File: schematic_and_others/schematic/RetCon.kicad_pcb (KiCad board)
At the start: 2 copper layers, 139.5 x 70.4 mm, 36 parts, among them J1 Hole1, J2 Hole2, J3 Hole3, J4 Hole4, J5 programming port, J6 USB_B_Micro, SW1 SW_SPDT, SW2 Home, SW3 BumperR, SW4 Select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

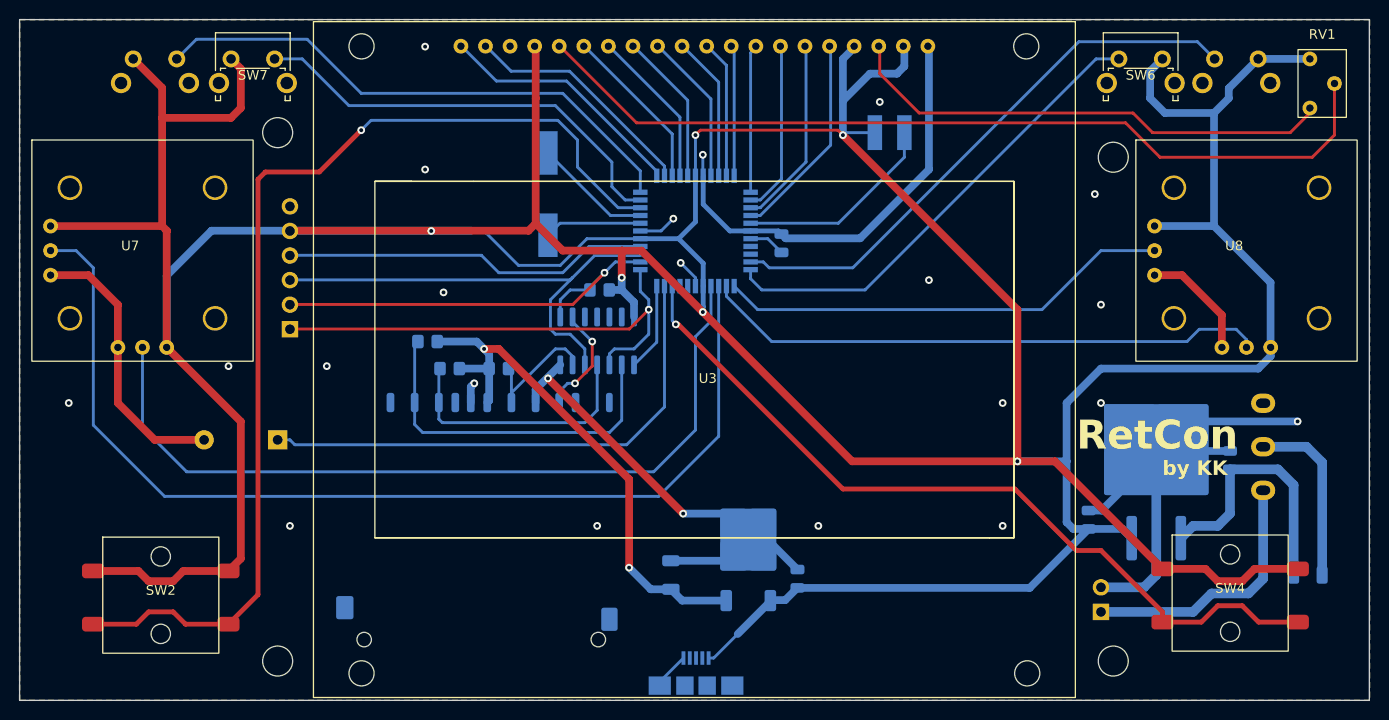
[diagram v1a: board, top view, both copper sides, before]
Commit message: Board update
- capacitors placed and connected
- buttons connected to ground
- need to update buttons and display footprints
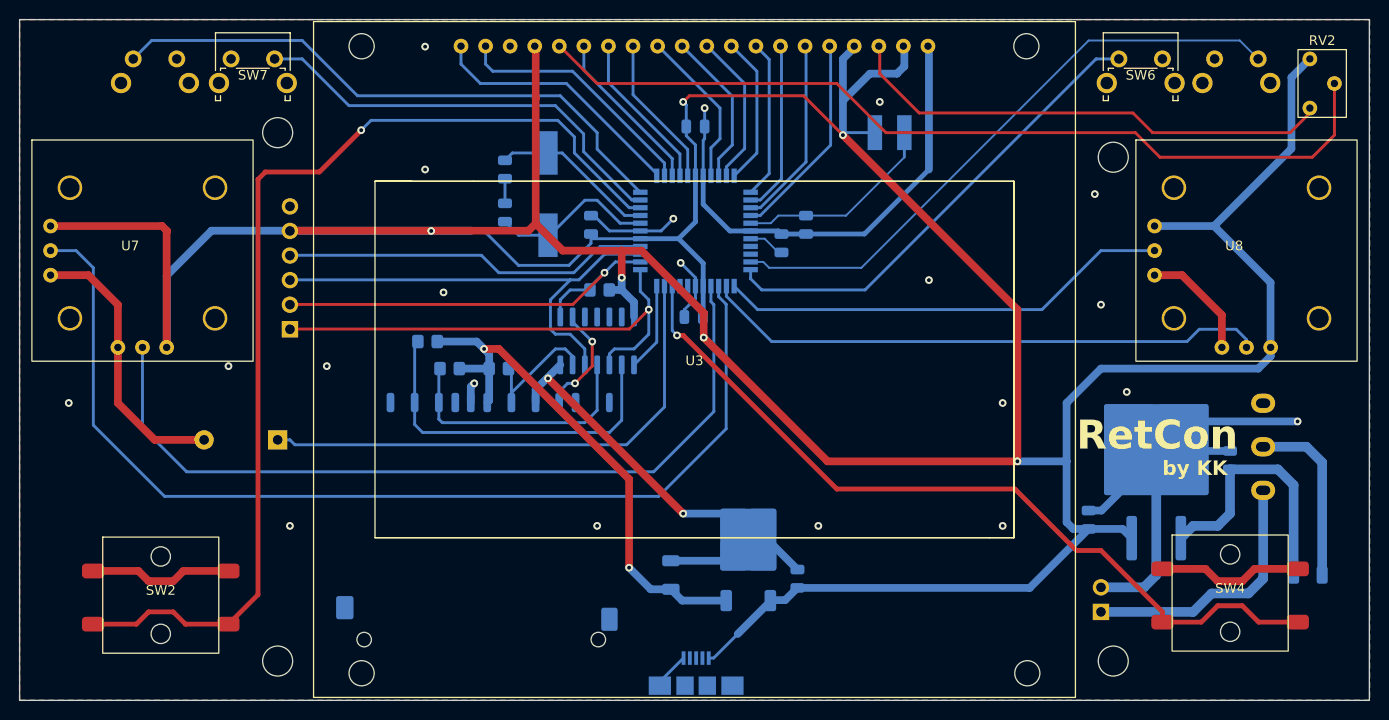
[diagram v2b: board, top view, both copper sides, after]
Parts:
- removed J6: USB_B_Micro, USB:USBMicro-SMD
- removed RV1: R_POT, Blue:potentiometer10K
- added C10: 100n, Capacitor_SMD:C_0805_2012Metric, B.Cu at (153.0, 70.5)
- added C11: 100n, Capacitor_SMD:C_0805_2012Metric, B.Cu at (175.3, 70.5)
- added C6: 22p, Capacitor_SMD:C_0805_2012Metric, B.Cu at (144.1, 64.8)
- added C7: 22p, Capacitor_SMD:C_0805_2012Metric, B.Cu at (144.1, 69.2)
- added C8: 100n, Capacitor_SMD:C_0805_2012Metric, B.Cu at (163.6, 80.0)
- added C9: 100n, Capacitor_SMD:C_0805_2012Metric, B.Cu at (163.8, 60.3)
- added J1: USB_B_Micro, USB:USBMicro-SMD, B.Cu at (163.9, 116.8)
- added RV2: R_Potentiometer, Blue:potentiometer10K, F.Cu at (228.6, 55.9)
- C2, C3, C5: value 100N -> 100n
- C4: value 2.2uF -> 2.2u
- J5: value programming port -> ~
- SW1: value SW_SPDT -> ON/OFF
- U1: value ATmega1284P -> ATmega1284P-A
- turned C5 to -90 degrees
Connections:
- net Net-(J5-Pin_4) renamed /RST
- net Net-(U1-PA0) renamed /LAnalogX
- net Net-(U1-PA1) renamed /LAnalogY
- net Net-(U1-PA2) renamed /RAnalogX
- net Net-(U1-PA3) renamed /RAnalogY
- net Net-(U1-PA4) renamed /TriggerR
- net Net-(U1-PB2) renamed /Select
- net Net-(U1-PC0) renamed /LCD_DATA0
- net Net-(U1-PC1) renamed /LCD_DATA1
- net Net-(U1-PC2) renamed /LCD_DATA2
- net Net-(U1-PC3) renamed /LCD_DATA3
- net Net-(U1-PC4) renamed /LCD_DATA4
- net Net-(U1-PC5) renamed /LCD_DATA5
- net Net-(U1-PC6) renamed /LCD_DATA6
- net Net-(U1-PC7) renamed /LCD_DATA7
- net Net-(U1-PD0) renamed /Home
- net Net-(U1-PD1) renamed /TriggerL
- net Net-(U1-PD3) renamed /LCD_CS1
- net Net-(U1-PD4) renamed /LCD_CS2
- net Net-(U1-PD5) renamed /LCD_RS
- net Net-(U1-PD6) renamed /LCD_RST
- net Net-(U1-PD7) renamed /LCD_E
- C5 pad 1: Net-(U1-AREF) -> GND
- C5 pad 2: GND -> Net-(U1-AREF)
- SW2 pad 1: +5V -> GND
- SW3 pad 1: +5V -> /BumperR
- SW3 pad 2: Net-(U1-PA5) -> GND
- SW4 pad 1: +5V -> GND
- SW5 pad 1: Net-(U1-PD2) -> GND
- SW5 pad 2: +5V -> /BumperL
- SW6 pad 2: +5V -> GND
- SW7 pad 1: +5V -> GND
- U1 pad 11: Net-(U1-PD2) -> /BumperL
- U1 pad 32: Net-(U1-PA5) -> /BumperR
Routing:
- net +5V: track 561.7 -> 449.9 mm
- net /BumperR: track 0.00 -> 63.2 mm
- net /BumperL: track 0.00 -> 60.7 mm
- net Net-(U1-PA5): track 58.6 -> 0.00 mm
- net Net-(U1-PD2): track 56.6 -> 0.00 mm
- net GND: track 196.1 -> 242.5 mm
- net Net-(U1-XTAL2): track 10.1 -> 17.0 mm
- net Net-(U1-XTAL1): track 12.2 -> 17.0 mm
- net /LCD_DATA3: track 13.4 -> 15.4 mm
- net /LCD_DATA2: track 14.1 -> 15.7 mm
- net /LCD_CS2: track 24.5 -> 25.9 mm
- net /LCD_DATA1: track 14.9 -> 16.1 mm
- net /LCD_DATA4: track 15.3 -> 16.5 mm
- net /LCD_CS1: track 25.9 -> 27.0 mm
- net /LCD_DATA0: track 15.6 -> 16.5 mm
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
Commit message: Board sent to manufacturer
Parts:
- moved U3 2.19 mm to (161.5, 84.5)
- moved L1 1.02 mm to (182.9, 61.0)
- renumbered RV2 to RV1
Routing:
- net GND: track 242.5 -> 248.8 mm, vias 23 -> 13
- net Net-(U3-V0): track 91.0 -> 94.6 mm
- net /LCD_DATA0: track 16.5 -> 20.0 mm
- net +5V: track 449.9 -> 446.5 mm
- net /LCD_DATA1: track 16.1 -> 18.9 mm
- net /LCD_CS1: track 27.0 -> 29.4 mm
- net /LCD_DATA2: track 15.7 -> 17.8 mm
- net /LCD_CS2: track 25.9 -> 27.9 mm
- net Net-(U3-VEE): track 51.1 -> 53.1 mm
- net /LCD_DATA5: track 17.8 -> 18.9 mm
- net /LCD_DATA3: track 15.4 -> 16.4 mm
- net /LCD_RST: track 16.5 -> 17.4 mm
- net /LCD_DATA4: track 16.5 -> 17.4 mm
- net /LCD_E: track 15.7 -> 16.6 mm
- net /LCD_RS: track 17.2 -> 18.1 mm
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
